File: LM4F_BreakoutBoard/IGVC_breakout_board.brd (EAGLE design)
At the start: 83.5 x 80 mm, 21 parts, among them IC1 7407N

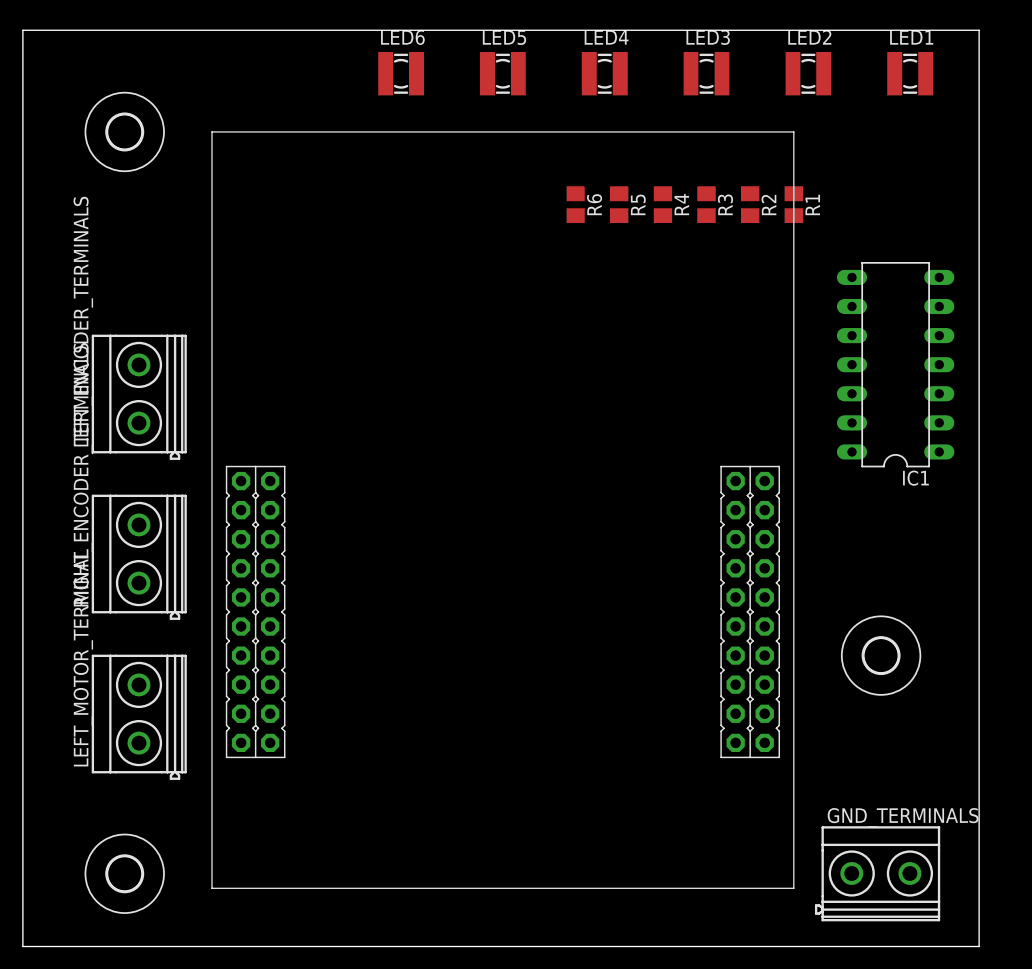
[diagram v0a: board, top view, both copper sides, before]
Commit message: Ground plane added and traces routed. First design iteration pretty much completed and ready to test.
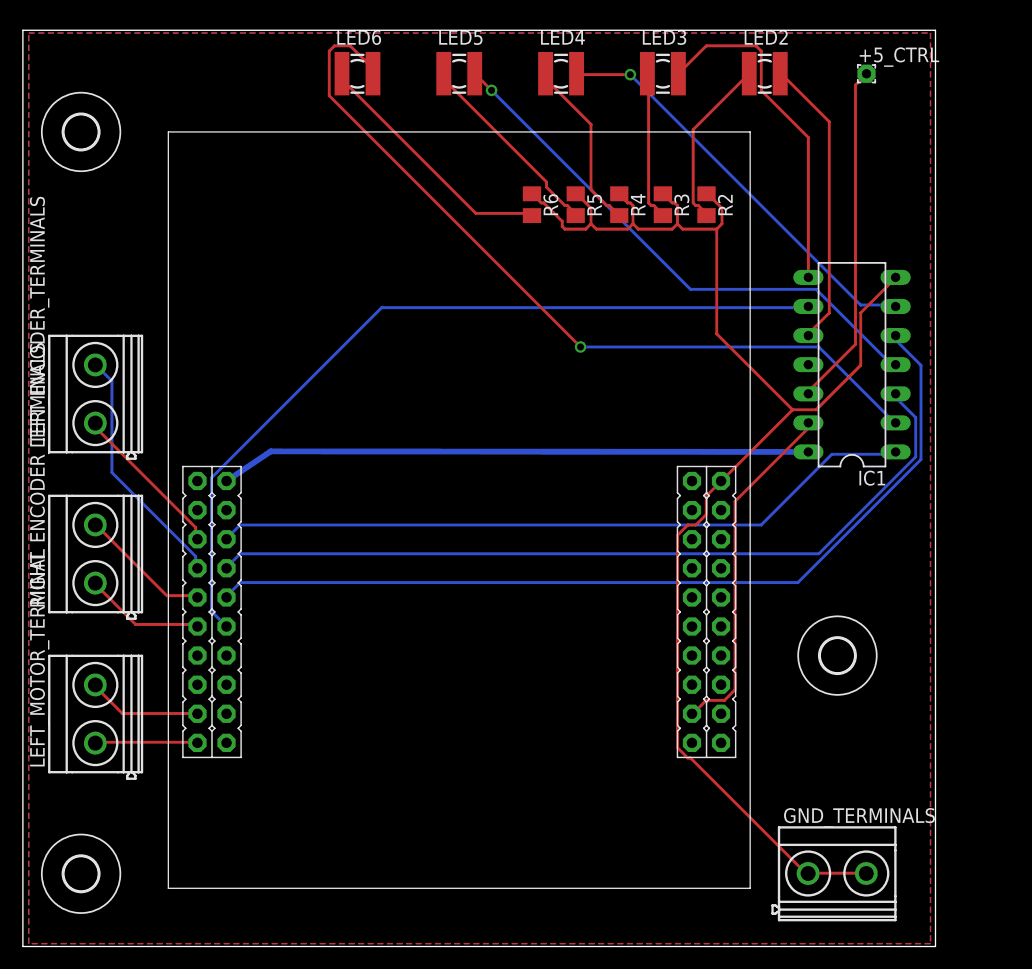
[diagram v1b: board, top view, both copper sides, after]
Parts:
- removed LED1: NFSG036BT, led:NFSG036BT
- removed R1: (no value), resistor:M0805
- added +5_CTRL: (no value), wirepad:1,6/0,8
- moved GND_TERMINALS 3.81 mm to (71.1, 6.35)
- moved H2 3.81 mm to (71.1, 25.4)
- moved IC1 3.81 mm to (72.4, 50.8)
- moved LED2 3.81 mm to (64.8, 76.2)
- moved LED6 3.81 mm to (29.2, 76.2)
- moved LM4F 3.81 mm to (12.7, 71.1)
- moved R2 3.81 mm to (59.7, 64.8)
- moved R4 3.81 mm to (52.1, 64.8)
- moved R5 3.81 mm to (48.3, 64.8)
- moved H4 3.81 mm to (5.08, 6.35)
- moved H5 3.81 mm to (5.08, 71.1)
- moved LEFT_ENCODER_TERMINALS 3.81 mm to (6.35, 48.3)
- moved LEFT_MOTOR_TERMINAL 3.81 mm to (6.35, 20.3)
- moved RIGHT_ENCODER_TERMINALS 3.81 mm to (6.35, 34.3)
- moved LED3 3.81 mm to (55.9, 76.2)
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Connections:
- removed net N$14: IC1.2, LED1.A
- new net N$7: IC1.14, LM4F.VBUS
- net GND: no longer IC1.14, LM4F.VBUS, R1.1
- net N$15: now also IC1.10; no longer IC1.4
- net N$16: now also IC1.8; no longer IC1.6
- net N$17: now also IC1.6; no longer IC1.8
- net N$18: now also IC1.4; no longer IC1.10
- net N$19: now also IC1.2; no longer IC1.12
- net N$20: now also IC1.1; no longer IC1.13
- net N$21: now also IC1.3; no longer IC1.11
- net N$22: now also IC1.5; no longer IC1.9
- net N$23: now also IC1.9; no longer IC1.5
- net N$25: now also IC1.13; no longer IC1.1
- net N$8: now also +5_CTRL.1, IC1.12; no longer LED1.C, R1.2
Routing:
- net GND: track 0.00 -> 122.5 mm
- net N$22: track 0.00 -> 77.4 mm
- net N$23: track 0.00 -> 71.9 mm
- net N$21: track 0.00 -> 70.5 mm
- net N$19: track 0.00 -> 70.5 mm, vias 0 -> 1
- net N$20: track 0.00 -> 61.7 mm
- net N$7: track 0.00 -> 51.7 mm
- net N$18: track 0.00 -> 47.3 mm, vias 0 -> 1
- net N$17: track 0.00 -> 36.3 mm, vias 0 -> 1
- net N$25: track 0.00 -> 30.6 mm
- net N$8: track 0.00 -> 30.0 mm
- net N$16: track 0.00 -> 29.9 mm
- net N$15: track 0.00 -> 25.4 mm
- net N$13: track 0.00 -> 22.0 mm
- net N$6: track 0.00 -> 21.5 mm
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- added copper zone on layer 1, net GND
- added copper zone on layer 16, net GND
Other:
- board size 83.5 x 80 mm -> 79.7 x 80 mm

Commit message: Basic silk screen added to label outputs
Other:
- board text added: "GND"
- board text added: "IEEE RAS IGVC 2015 LM4F Breakout Board"
- board text added: "Left Encoder"
- board text added: "Motor Out"
- board text added: "PD0"
- board text added: "PD1"
- board text added: "PD2"
- board text added: "PD3"
- board text added: "PD4"
- board text added: "PD5"
- board text added: "Right Encoder"
